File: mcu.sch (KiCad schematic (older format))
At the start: 75 parts, among them J11 RJ45_Shielded, J13 HR911105A, J2 RJ45_Shielded, U3 STM32F207VGT6, U4 MCP2562-E-P, U5 LAN8720A, Y1 Crystal_GND24

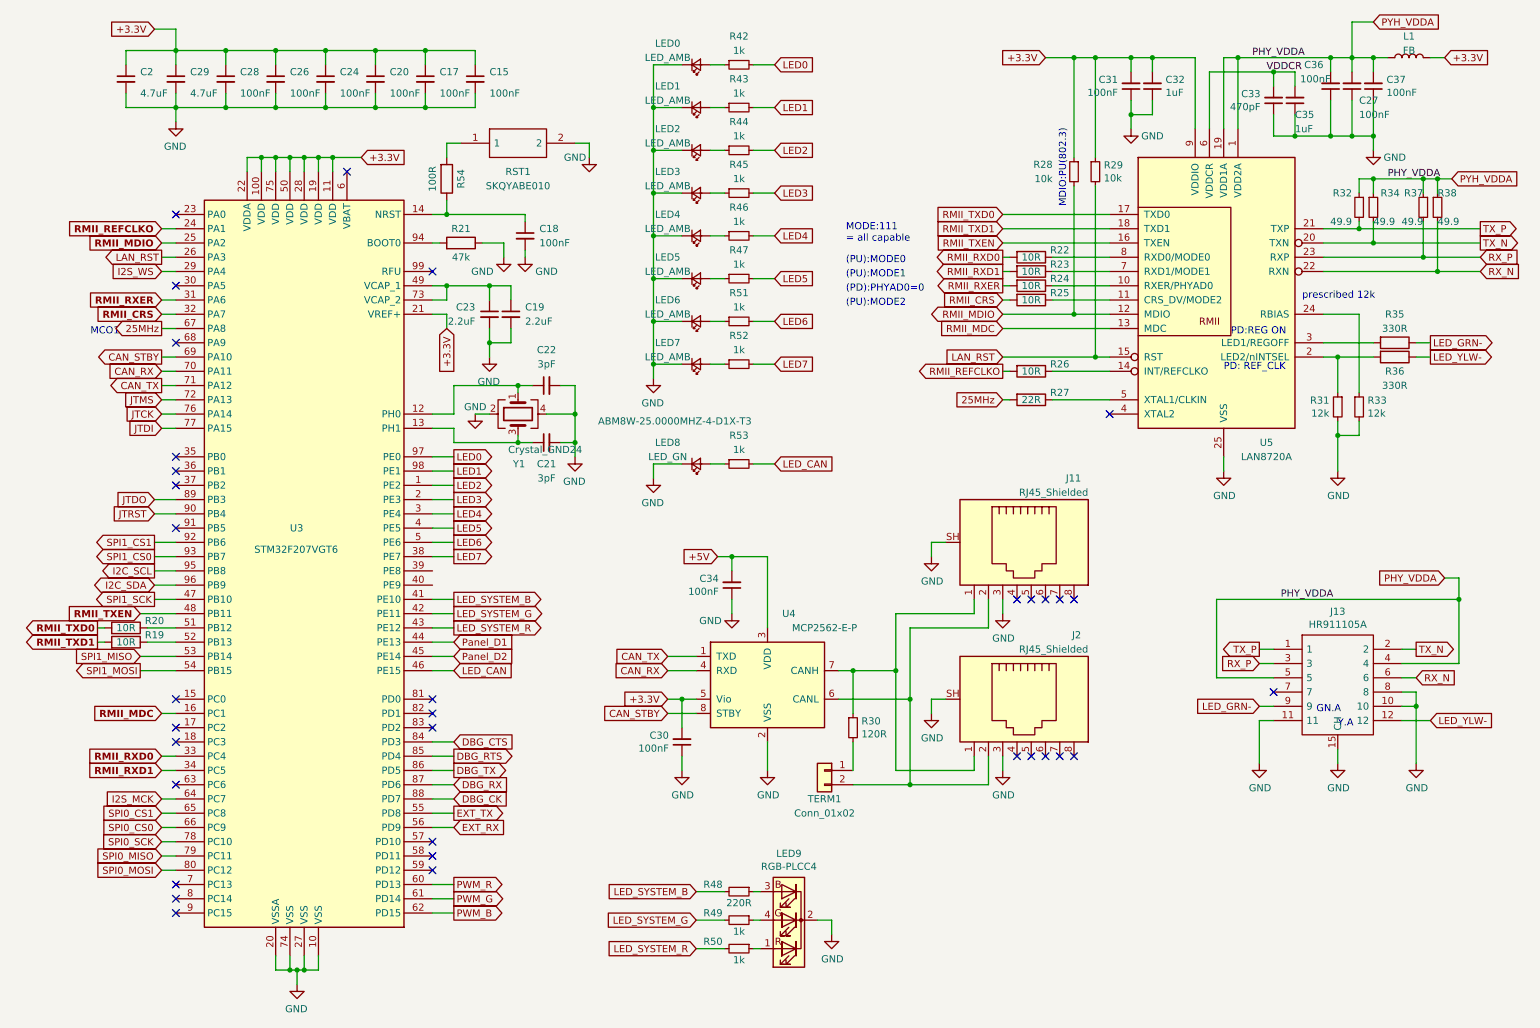
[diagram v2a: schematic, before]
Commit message: pinout validated against CubeMX listing (.ioc added), some nets renamed, system RGB LED reconnected. Reconnected I2C lines to include CAN alternate function. Warning: * bottom silkscreen labels might be invalidated
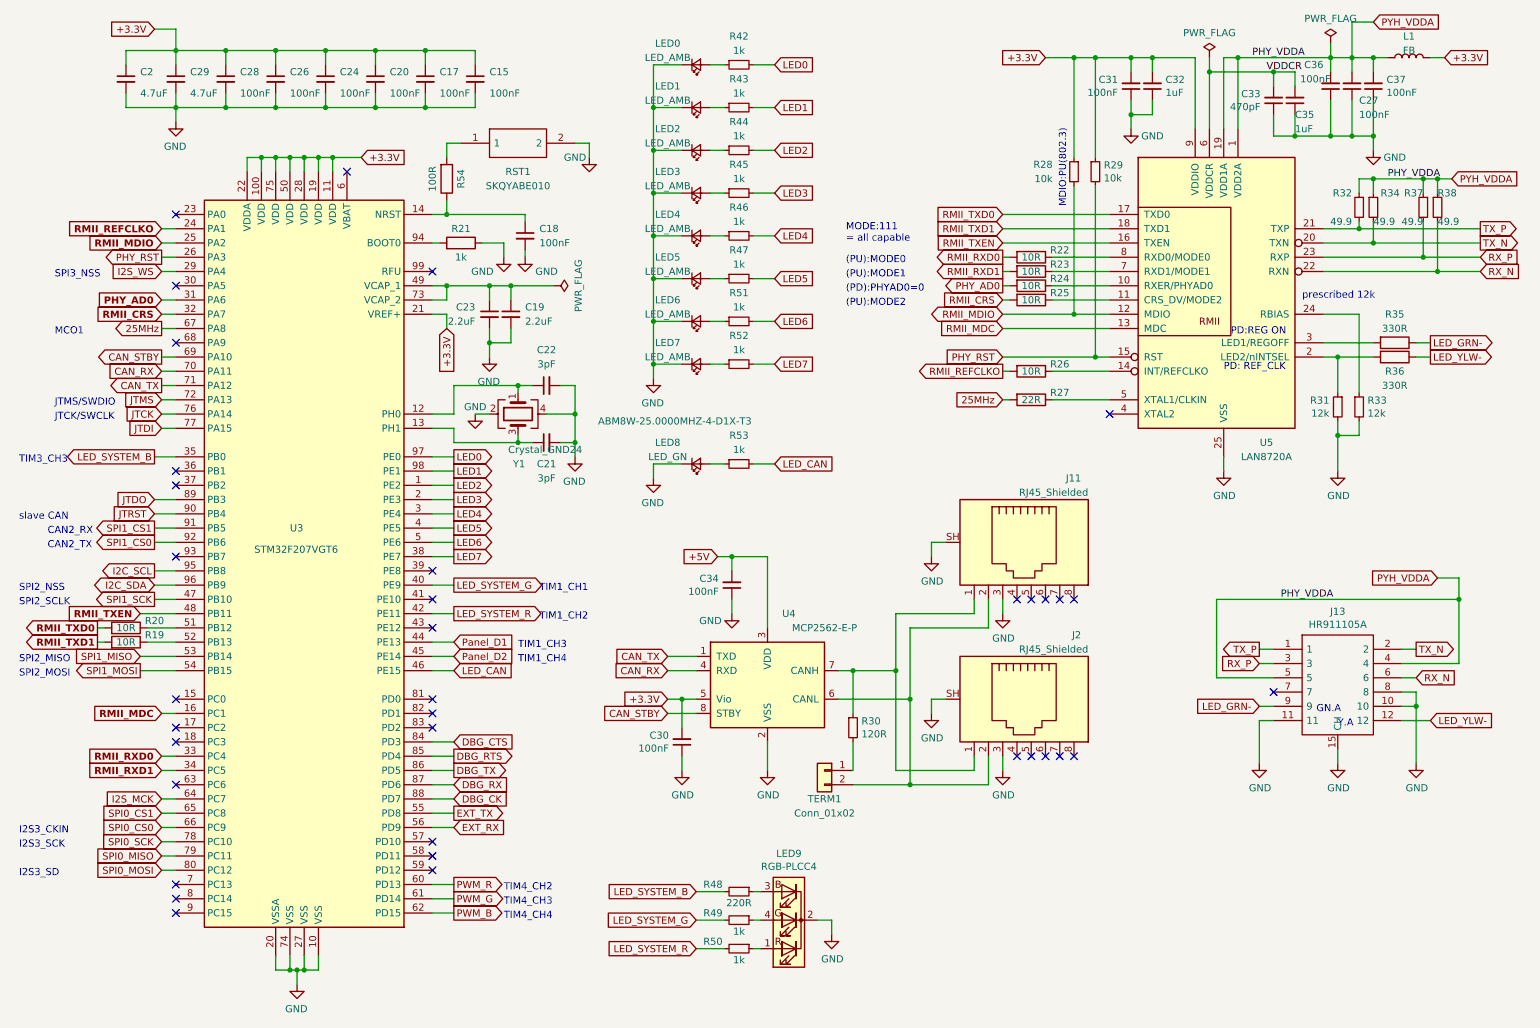
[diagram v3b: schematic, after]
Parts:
- R21: value 47k -> 1k
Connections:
- net LED_SYSTEM_B: now also U3.35 (PB0); no longer U3.41 (PE10)
- net LED_SYSTEM_G: now also U3.40 (PE9); no longer U3.42 (PE11)
- net LED_SYSTEM_R: now also U3.42 (PE11); no longer U3.43 (PE12)
- net SPI1_CS0: now also U3.92 (PB6); no longer U3.93 (PB7)
- net SPI1_CS1: now also U3.91 (PB5); no longer U3.92 (PB6)
- net LAN_RST renamed PHY_RST
- net PHY_VDDA renamed PYH_VDDA
- net RMII_RXER renamed PHY_AD0
- no-connect marks 34 -> 36
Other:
- note added: "CAN2_RX"
- note added: "CAN2_TX"
- note added: "I2S3_CKIN"
- note added: "I2S3_SCK"
- note added: "I2S3_SD"
- note added: "JTCK/SWCLK"
- note added: "JTMS/SWDIO"
- note added: "SPI2_MISO"
- note added: "SPI2_MOSI"
- note added: "SPI2_NSS"
- note added: "SPI2_SCLK"
- note added: "SPI3_NSS"
- note added: "TIM1_CH1"
- note added: "TIM1_CH2"
- note added: "TIM1_CH3"
- note added: "TIM1_CH4"
- note added: "TIM3_CH3"
- note added: "TIM4_CH2"
- note added: "TIM4_CH3"
- note added: "TIM4_CH4"
- note added: "slave CAN"
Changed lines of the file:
@@
 RMII_RXD1
 Text GLabel 7400 2500 0    50   Output ~ 0
-RMII_RXER
+PHY_AD0
 Text GLabel 7400 2600 0    50   Input ~ 0
 RMII_CRS
@@
 RMII_REFCLKO
 Text GLabel 7400 3000 0    50   Input ~ 0
-LAN_RST
+PHY_RST
 $Comp
 L Device:R_Small R28
@@
 Wire Wire Line
 	8900 4700 10600 4700
-Text GLabel 10500 4550 0    50   Input ~ 0
-PHY_VDDA
-Wire Wire Line
-	10500 4550 10600 4550
-Wire Wire Line
-	10600 4550 10600 4700
 Text GLabel 10400 2900 2    50   Output ~ 0
 LED_GRN-
@@
 RMII_TXD1
 Text GLabel 1500 2300 0    50   Output ~ 0
-LAN_RST
+PHY_RST
 Text GLabel 1500 2200 0    50   Input ~ 10
 RMII_MDIO
@@
 RMII_MDC
 Text GLabel 1500 2600 0    50   Input ~ 10
-RMII_RXER
+PHY_AD0
 Wire Wire Line
 	1500 2400 1600 2400
@@
 Wire Wire Line
 	1500 2800 1600 2800
-Text Notes 1000 2850 0    50   ~ 0
+Text Notes 750  2850 0    50   ~ 0
 MCO1
 $Comp
@@
 Text GLabel 1450 4700 0    50   Output ~ 0
 SPI1_SCK
-Text GLabel 1450 4400 0    50   Output ~ 0
+Text GLabel 1450 4300 0    50   Output ~ 0
 SPI1_CS0
-Text GLabel 1450 4300 0    50   Output ~ 0
+Text GLabel 1450 4200 0    50   Output ~ 0
 SPI1_CS1
 Wire Wire Line
-	1450 4400 1600 4400
-Wire Wire Line
-	1600 4300 1450 4300
+	1450 4300 1600 4300
+Wire Wire Line
+	1600 4200 1450 4200
 Wire Wire Line
 	1450 4700 1600 4700
@@
 NoConn ~ 1600 2900
 NoConn ~ 1600 2000
-NoConn ~ 1600 3700
+NoConn ~ 3400 4900
 NoConn ~ 1600 3800
 NoConn ~ 1600 3900
-NoConn ~ 1600 4200
+NoConn ~ 1600 4400
 NoConn ~ 1600 5400
 NoConn ~ 1600 5600
@@
 AR Path="/5C211FC6/5CF93D60" Ref="R?"  Part="1"
 F 0 "R21" V 3700 2200 50  0000 C CNN
-F 1 "47k" V 3500 2200 50  0000 C CNN
+F 1 "1k" V 3500 2200 50  0000 C CNN
 F 2 "Resistor_SMD:R_0603_1608Metric" V 3530 2200 50  0001 C CNN
 F 3 "~" H 3600 2200 50  0001 C CNN
@@
 Wire Wire Line
 	10600 5150 10600 4700
-Connection ~ 10600 4700
 $Comp
 L power:GND #PWR015
@@
 	2300 1600 2200 1600
 Connection ~ 2300 1600
-Wire Wire Line
-	2400 1600 2300 1600
-Connection ~ 2400 1600
-Wire Wire Line
-	2500 1600 2400 1600
-Connection ~ 2500 1600
-Wire Wire Line
-	2600 1600 2500 1600
 Connection ~ 2600 1600
 Wire Wire Line
@@
 	3550 3200 4000 3200
 Wire Wire Line
-	3550 4900 3400 4900
-Wire Wire Line
-	3400 4800 3550 4800
-Wire Wire Line
-	3550 4700 3400 4700
+	3550 4800 3400 4800
+Wire Wire Line
+	3400 4600 3550 4600
+Wire Wire Line
+	1450 3700 1600 3700
 Wire Wire Line
 	3400 4400 3550 4400
@@
 Text GLabel 3550 4100 2    50   Output ~ 0
 LED4
-Text GLabel 3550 4700 2    50   Output ~ 0
+Text GLabel 1450 3700 0    50   Output ~ 0
 LED_SYSTEM_B
+Text GLabel 3550 4600 2    50   Output ~ 0
+LED_SYSTEM_G
 Text GLabel 3550 4800 2    50   Output ~ 0
-LED_SYSTEM_G
-Text GLabel 3550 4900 2    50   Output ~ 0
 LED_SYSTEM_R
 Text GLabel 3550 3700 2    50   Output ~ 0
@@
 Wire Wire Line
 	3500 1500 3500 1600
+Connection ~ 2500 1600
+Connection ~ 2400 1600
+Wire Wire Line
+	2400 1600 2300 1600
+Wire Wire Line
+	2500 1600 2400 1600
+Wire Wire Line
+	2600 1600 2500 1600
+NoConn ~ 3400 4500
+NoConn ~ 3400 4700
+Text Notes 750  3350 0    50   ~ 0
+JTMS/SWDIO
+Text Notes 750  3450 0    50   ~ 0
+JTCK/SWCLK
+$Comp
+L power:PWR_FLAG #FLG?
+U 1 1 5BFBC076
+P 8850 900
+AR Path="/5BFBC076" Ref="#FLG?"  Part="1"
+AR Path="/5BBC4BB7/5BFBC076" Ref="#FLG0105"  Part="1"
+F 0 "#FLG0105" H 8850 975 50  0001 C CNN
+F 1 "PWR_FLAG" H 8850 1074 50  0000 C CNN
+F 2 "" H 8850 900 50  0001 C CNN
+F 3 "~" H 8850 900 50  0001 C CNN
+	1    8850 900
+	1    0    0    -1
+$EndComp
+$Comp
+L power:PWR_FLAG #FLG?
+U 1 1 5BFE35F6
+P 9700 800
+AR Path="/5BFE35F6" Ref="#FLG?"  Part="1"
+AR Path="/5BBC4BB7/5BFE35F6" Ref="#FLG0106"  Part="1"
+F 0 "#FLG0106" H 9700 875 50  0001 C CNN
+F 1 "PWR_FLAG" H 9700 974 50  0000 C CNN
+F 2 "" H 9700 800 50  0001 C CNN
+F 3 "~" H 9700 800 50  0001 C CNN
+	1    9700 800
+	1    0    0    -1
+$EndComp
+Wire Wire Line
+	9700 800  9700 900
+$Comp
+L power:PWR_FLAG #FLG?
+U 1 1 5C0B7824
+P 4250 2500
+AR Path="/5C0B7824" Ref="#FLG?"  Part="1"
+AR Path="/5BBC4BB7/5C0B7824" Ref="#FLG0107"  Part="1"
+F 0 "#FLG0107" H 4250 2575 50  0001 C CNN
+F 1 "PWR_FLAG" H 4250 2674 50  0000 C CNN
+F 2 "" H 4250 2500 50  0001 C CNN
+F 3 "~" H 4250 2500 50  0001 C CNN
+	1    4250 2500
+	0    1    1    0
+$EndComp
+Wire Wire Line
+	4250 2500 3950 2500
+Connection ~ 3950 2500
+Wire Wire Line
+	8850 900  8850 1000
+Connection ~ 8850 1000
+Text GLabel 10450 4550 0    50   Input ~ 0
+PYH_VDDA
+Wire Wire Line
+	10450 4550 10600 4550
+Wire Wire Line
+	10600 4550 10600 4700
+Connection ~ 10600 4700
+Text Notes 700  4250 0    50   ~ 0
+CAN2_RX
+Text Notes 700  4350 0    50   ~ 0
+CAN2_TX
+Text Notes 500  4150 0    50   ~ 0
+slave CAN
+Text Notes 500  6650 0    50   ~ 0
+I2S3_SD
+Text Notes 500  6450 0    50   ~ 0
+I2S3_SCK
+Text Notes 500  6350 0    50   ~ 0
+I2S3_CKIN
+Text Notes 750  2450 0    50   ~ 0
+SPI3_NSS
+Text Notes 500  4750 0    50   ~ 0
+SPI2_SCLK
+Text Notes 500  5250 0    50   ~ 0
+SPI2_MOSI
+Text Notes 500  5150 0    50   ~ 0
+SPI2_MISO
+Text Notes 500  4650 0    50   ~ 0
+SPI2_NSS
+Text Notes 4000 5050 0    50   ~ 0
+TIM1_CH3
+Text Notes 4000 5150 0    50   ~ 0
+TIM1_CH4
+Text Notes 3900 6750 0    50   ~ 0
+TIM4_CH2
+Text Notes 3900 6850 0    50   ~ 0
+TIM4_CH3
+Text Notes 3900 6950 0    50   ~ 0
+TIM4_CH4
+Text Notes 500  3750 0    50   ~ 0
+TIM3_CH3
+Text Notes 4150 4650 0    50   ~ 0
+TIM1_CH1
+Text Notes 4150 4850 0    50   ~ 0
+TIM1_CH2
 $EndSCHEMATC

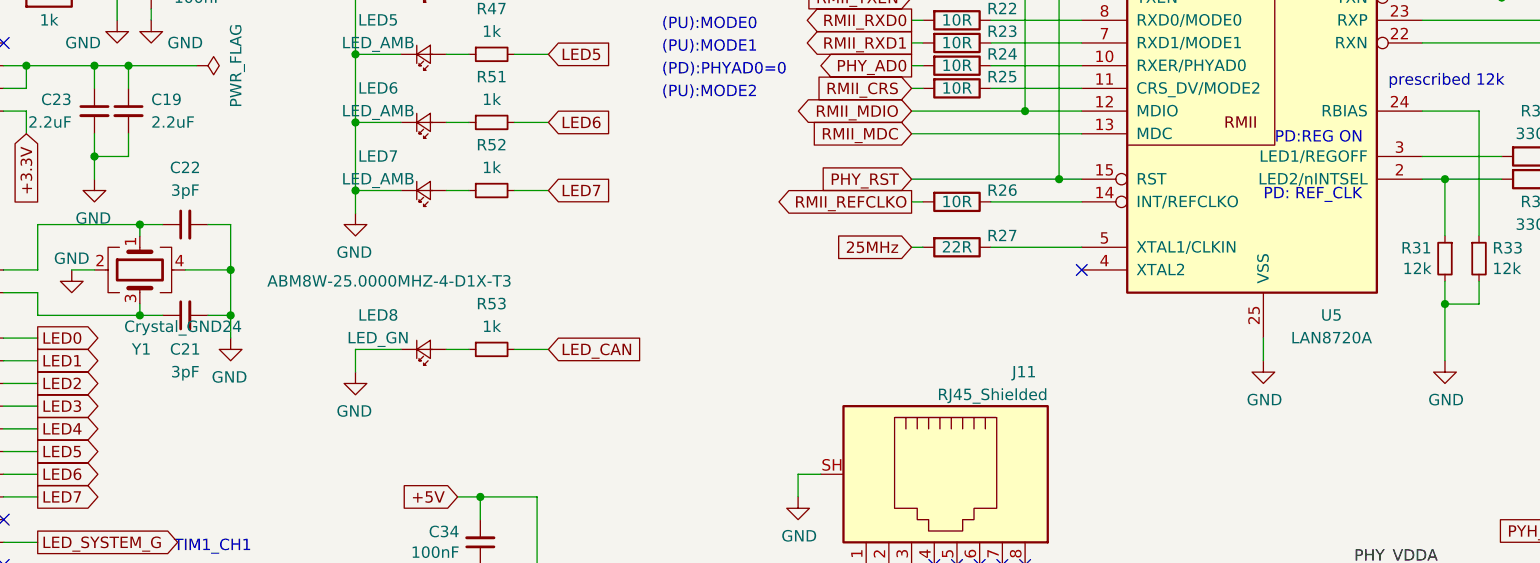
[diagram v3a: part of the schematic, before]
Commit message: swap xtal for 12 MHz type with CL=8pF -> 2MHz PLL in (optimum), larger load capacitors offering higher noise immunity, HSE gain margin should still be ok, silk screen changes due to secondary CAN interface mapping to CS0+CS1 pins, system LED reconnected to TIM1+TIM3 PWM channels for ease of use. Migrated LAN8720A to pin / alternate function compatible LAN8742A. Details see migration guide http://ww1.microchip.com/downloads/en/AppNotes/en562713.pdf. Schematic and layout validation done. Note SPI0 and SPI1 refer to SPI2 and SPI3 peripherals... we'll have to see how much of an annoyance this turns out to be :) [this version is released to production]
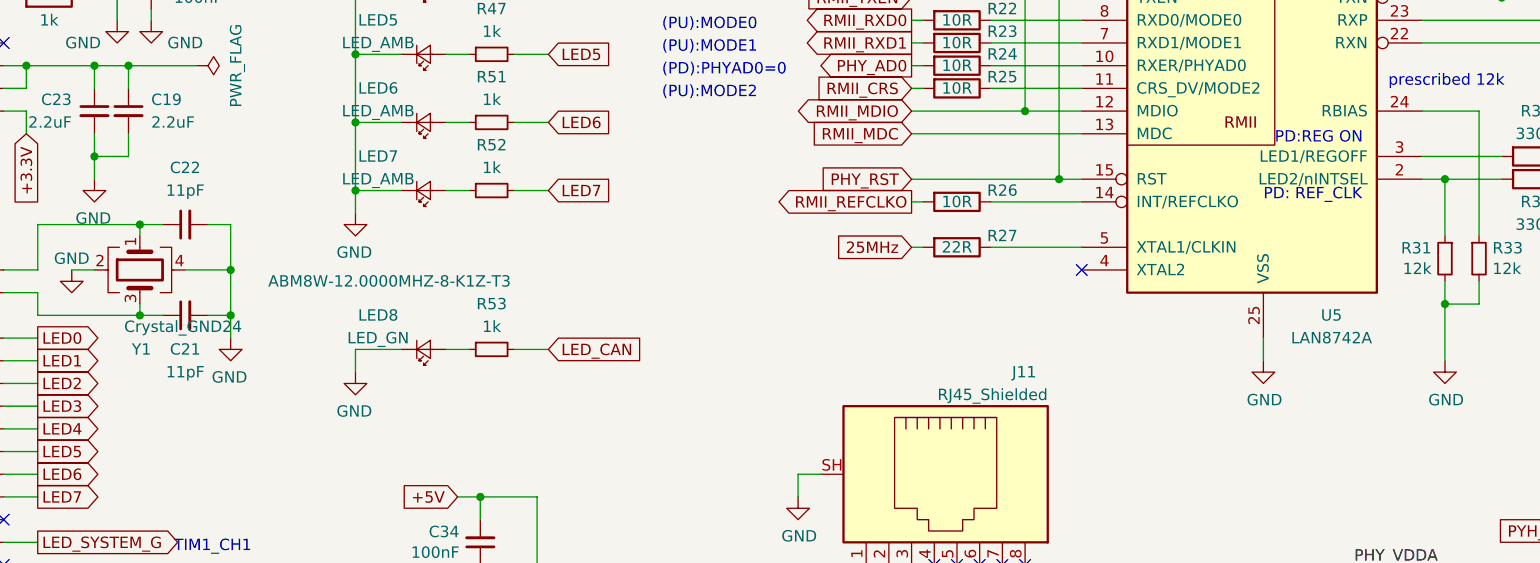
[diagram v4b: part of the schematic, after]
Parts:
- C21, C22: value 3pF -> 11pF; MPN CC603CRNPO9BN3R0 / C1608C0G2A030C080AA -> CBR06C110F5GAC; Mouser 603-CC603CRNPO9BN3R0 / 810-C1608C0G2A030C0A -> 80-CBR06C110F5G
- U5: value LAN8720A -> LAN8742A; MPN LAN8720A-CP-TR-ABC -> LAN8742A-CZ-TR; Mouser 579-LAN8720ACPTRABC -> 579-LAN8742A-CZ-TR
- Y1: MPN ABM8W-25.0000MHZ-4-D1X-T3 -> ABM8W-12.0000MHZ-8-K1Z-T3; Mouser 815-8W25-4D1XT -> 815-8W12-8K1ZT
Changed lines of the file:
@@
 AR Path="/5C211FC6/5BBD20DE" Ref="U?"  Part="1"
 F 0 "U5" H 9250 1600 50  0000 C CNN
-F 1 "LAN8720A" H 9250 1500 50  0000 C CNN
+F 1 "LAN8742A" H 9250 1500 50  0000 C CNN
 F 2 "Package_DFN_QFN:QFN-24-1EP_4x4mm_P0.5mm_EP2.6x2.6mm" H 9000 1650 50  0001 L CNN
 F 3 "http://ww1.microchip.com/downloads/en/DeviceDoc/8720a.pdf" H 8750 1650 50  0001 C CNN
-F 4 "LAN8720A-CP-TR-ABC" H 8950 2600 50  0001 C CNN "MPN"
-F 5 "579-LAN8720ACPTRABC" H 8950 2600 50  0001 C CNN "Mouser"
+F 4 "LAN8742A-CZ-TR" H 8950 2600 50  0001 C CNN "MPN"
+F 5 "579-LAN8742A-CZ-TR" H 8950 2600 50  0001 C CNN "Mouser"
 	1    8950 2600
 	1    0    0    -1
@@
 F 2 "Crystal:Crystal_SMD_Abracon_ABM8G-4Pin_3.2x2.5mm" H 4000 3400 50  0001 C CNN
 F 3 "~" H 4000 3400 50  0001 C CNN
-F 4 "ABM8W-25.0000MHZ-4-D1X-T3" V 4050 2300 50  0000 C CNN "MPN"
-F 5 "815-8W25-4D1XT" V 4000 3400 50  0001 C CNN "Mouser"
+F 4 "ABM8W-12.0000MHZ-8-K1Z-T3" V 4050 2300 50  0000 C CNN "MPN"
+F 5 "815-8W12-8K1ZT" V 4000 3400 50  0001 C CNN "Mouser"
 	1    4000 3400
 	0    -1   1    0
@@
 AR Path="/5C211FC6/5BCAE054" Ref="C?"  Part="1"
 F 0 "C22" V 3950 3200 50  0000 C CNN
-F 1 "3pF" V 4050 3200 50  0000 C CNN
+F 1 "11pF" V 4050 3200 50  0000 C CNN
 F 2 "Capacitor_SMD:C_0603_1608Metric" H 4200 3200 50  0001 C CNN
 F 3 "~" H 4200 3200 50  0001 C CNN
-F 4 "CC603CRNPO9BN3R0 / C1608C0G2A030C080AA " V 4200 3200 50  0001 C CNN "MPN"
-F 5 "603-CC603CRNPO9BN3R0 / 810-C1608C0G2A030C0A " V 4200 3200 50  0001 C CNN "Mouser"
+F 4 "CBR06C110F5GAC" V 4200 3200 50  0001 C CNN "MPN"
+F 5 "80-CBR06C110F5G" V 4200 3200 50  0001 C CNN "Mouser"
 	1    4200 3200
 	0    -1   1    0
@@
 AR Path="/5C211FC6/5DEBCA55" Ref="C?"  Part="1"
 F 0 "C21" V 4050 3600 50  0000 C CNN
-F 1 "3pF" V 3950 3600 50  0000 C CNN
+F 1 "11pF" V 3950 3600 50  0000 C CNN
 F 2 "Capacitor_SMD:C_0603_1608Metric" H 4200 3600 50  0001 C CNN
 F 3 "~" H 4200 3600 50  0001 C CNN
-F 4 "CC603CRNPO9BN3R0 / C1608C0G2A030C080AA " V 4200 3600 50  0001 C CNN "MPN"
-F 5 "603-CC603CRNPO9BN3R0 / 810-C1608C0G2A030C0A " V 4200 3600 50  0001 C CNN "Mouser"
+F 4 "CBR06C110F5GAC" V 4200 3600 50  0001 C CNN "MPN"
+F 5 "80-CBR06C110F5G" V 4200 3600 50  0001 C CNN "Mouser"
 	1    4200 3600
 	0    -1   -1   0

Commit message: BOM DONE
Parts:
- C15, C17, C18, C20, C24, C26, C27, C28, C30, C31, C34, C36, C37: MPN (none) -> C0603C104K5RECAUTO; Mouser (none) -> 80-C0603C104K5REAUTO
- C19, C23: MPN (none) -> 885012106011; Mouser (none) -> 710-885012106011
- C2, C29: MPN (none) -> GRM21BR71A475KE51L; Mouser (none) -> 81-GRM21BR71A475KE1L
- C32, C35: value 1uF -> 2.2uF; MPN (none) -> 885012106011; Mouser (none) -> 710-885012106011
- C33: value 470pF -> 10nF; MPN (none) -> C0603C103K1REAUTO; Mouser (none) -> 80-C0603C103K1REAUTO
- J13: Mouser 710-7499011121A (WE equivalent) -> 710-7499011121A (WE near match)
- LED1, LED2, LED3, LED4, LED5, LED6, LED7: MPN (none) -> LTST-C190AKT; Mouser (none) -> 859-LTST-C190AKT
- LED8: MPN (none) -> LTST-C190KGKT; Mouser (none) -> 859-LTST-C190KGKT
- R19, R20, R22, R23, R24, R25, R26: value 10R -> 22R; MPN (none) -> RC0603JR-0722RL; Mouser (none) -> 603-RC0603JR-0722RL
- R21, R42, R43, R44, R45, R46, R47, R49, R50, R51, R52, R53: MPN (none) -> RC0603FR-071KL; Mouser (none) -> 603-RC0603FR-071KL
- R27: MPN (none) -> RC0603JR-0722RL; Mouser (none) -> 603-RC0603JR-0722RL
- R28, R29: value 10k -> 12k; MPN (none) -> RC0603FR-0712KL; Mouser (none) -> 603-RC0603FR-0712KL
- R30: MPN (none) -> RC0603FR-07120RL; Mouser (none) -> 603-RC0603FR-07120RL
- R31, R33: MPN (none) -> RC0603FR-0712KL; Mouser (none) -> 603-RC0603FR-0712KL
- R32, R34, R37, R38: MPN (none) -> RC0603FR-0749R9L; Mouser (none) -> 603-RC0603FR-0749R9L
- R35, R36: value 330R -> 1k; MPN (none) -> RC0603FR-071KL; Mouser (none) -> 603-RC0603FR-071KL
- R48: value 220R -> 120R; MPN (none) -> RC0603FR-07120RL; Mouser (none) -> 603-RC0603FR-07120RL
- R54: value 100R -> 120R; MPN (none) -> RC0603FR-07120RL; Mouser (none) -> 603-RC0603FR-07120RL
- TERM1: DigiKey (none) -> 455-1719-ND; MPN (none) -> S2B-PH-K-S(LF)(SN)‎

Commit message: BOM completed, inventory checked and listed in BOM. Adds project diagram.
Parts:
- C15, C17, C18, C2, C20, C24, C26, C27, C28, C29, C30, C31, C33, C34, C36, C37, J13, R19, R20, R21, R22, R23, R24, R25, R26, R27, R28, R29, R30, R31, R33, R35, R36, R42, R43, R44, R45, R46, R47, R48, R49, R50, R51, R52, R53, R54, RST1, TERM1: stock (none) -> X
- J11, J2, U5: stock (none) -> (X)
